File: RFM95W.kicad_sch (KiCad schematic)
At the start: 2 parts

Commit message: ongoing add MCU and radio.
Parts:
- added AE1: 915mhz antenna, ProjectLib:915MHz_spring_antenna, symbol Device:Antenna
- R?: value 10k -> 10k 1%
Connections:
- net ANT: no longer names the net of U?.9 (ANT)
- net ANT: now also AE1.1 (A)

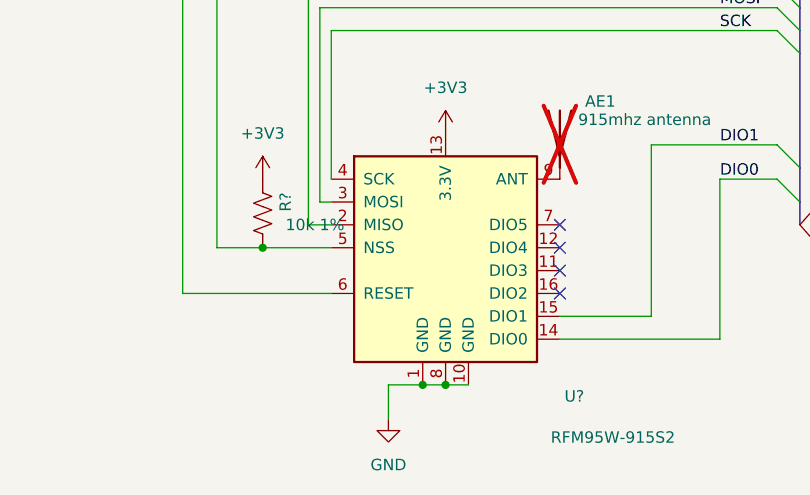
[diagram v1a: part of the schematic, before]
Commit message: ERC passing, Crytals not specified. Considering reverse polarity safeguard.
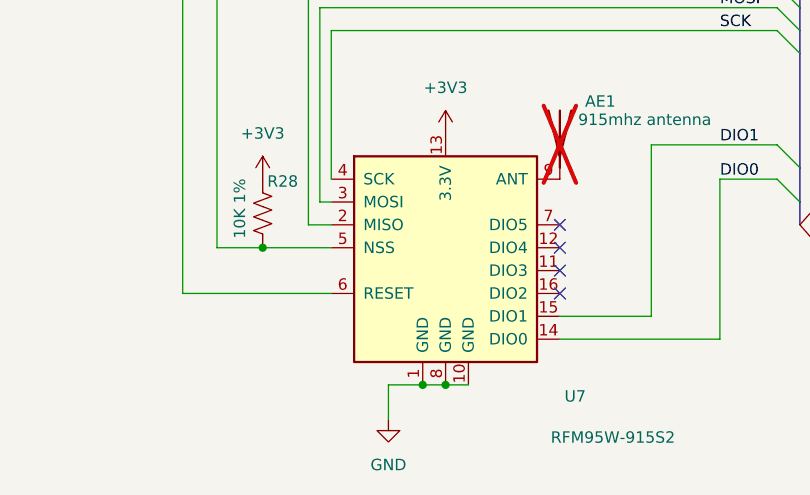
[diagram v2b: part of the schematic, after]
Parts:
- removed R?: 10k 1%, ProjectLib:R_0603_1608Metric, symbol ProjectLib:R_US
- added R28: 10K 1%, symbol Device:R_US
- gave numbers to parts that had none: 1
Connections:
- net +3V3: now also R28.1
- net NSS: now also R28.2
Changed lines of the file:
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@@
+	)
+	(junction
+		(at 115.57 100.33)
+		(diameter 0)
+		(color 0 0 0 0)
 	)
 	(junction
@@
 		(color 0 0 0 0)
 	)
-	(junction
-		(at 115.57 100.33)
-		(diameter 0)
-		(color 0 0 0 0)
-	)
 	(no_connect
 		(at 128.27 87.63)
@@
 		)
 	)
-	(wire
-		(pts
-			(xy 95.25 85.09) (xy 90.17 85.09)
-		)
-		(stroke
-			(width 0)
-			(type default)
-		)
-	)
 	(bus
 		(pts
@@
 	(wire
 		(pts
-			(xy 102.87 85.09) (xy 95.25 85.09)
-		)
-		(stroke
-			(width 0)
-			(type default)
-		)
-	)
-	(wire
-		(pts
 			(xy 102.87 82.55) (xy 100.33 82.55)
 		)
@@
 		(pts
 			(xy 154.94 80.01) (xy 154.94 82.55)
+		)
+		(stroke
+			(width 0)
+			(type default)
+		)
+	)
+	(wire
+		(pts
+			(xy 95.25 85.09) (xy 102.87 85.09)
+		)
+		(stroke
+			(width 0)
+			(type default)
+		)
+	)
+	(wire
+		(pts
+			(xy 90.17 85.09) (xy 95.25 85.09)
 		)
 		(stroke
@@
 	)
 	(symbol
+		(lib_id "Device:R_US")
+		(at 95.25 81.28 0)
+		(unit 1)
+		(exclude_from_sim no)
+		(in_bom yes)
+		(on_board yes)
+		(dnp no)
+		(property "Reference" "R28"
+			(at 95.758 77.724 0)
+			(effects
+				(font
+					(size 1.27 1.27)
+				)
+				(justify left)
+			)
+		)
+		(property "Value" "10K 1%"
+			(at 92.71 84.074 90)
+			(effects
+				(font
+					(size 1.27 1.27)
+				)
+				(justify left)
+			)
+		)
+		(property "Footprint" ""
+			(at 96.266 81.534 90)
+			(effects
+				(font
+					(size 1.27 1.27)
+				)
+				(hide yes)
+			)
+		)
+		(property "Datasheet" "~"
+			(at 95.25 81.28 0)
+			(effects
+				(font
+					(size 1.27 1.27)
+				)
+				(hide yes)
+			)
+		)
+		(property "Description" "Resistor, US symbol"
+			(at 95.25 81.28 0)
+			(effects
+				(font
+					(size 1.27 1.27)
+				)
+				(hide yes)
+			)
+		)
+		(pin "2"
+		)
+		(pin "1"
+		)
+		(instances
+			(project ""
+				(path "/0c2d0c14-8850-4a30-bb78-b2f40cb442ba/2db29b35-1005-45eb-b852-0b853354466f"
+					(reference "R28")
+					(unit 1)
+				)
+			)
+		)
+	)
+	(symbol
 		(lib_id "power:+3V3")
 		(at 95.25 77.47 0)
@@
 		(dnp no)
 		(fields_autoplaced yes)
-		(property "Reference" "#PWR?"
+		(property "Reference" "#PWR0102"
 			(at 95.25 81.28 0)
 			(effects
@@
 			(project "SensorProject_t16-pcb"
 				(path "/0c2d0c14-8850-4a30-bb78-b2f40cb442ba/2db29b35-1005-45eb-b852-0b853354466f"
-					(reference "#PWR?")
+					(reference "#PWR0102")
 					(unit 1)
 				)
@@
 		(dnp no)
 		(fields_autoplaced yes)
-		(property "Reference" "#PWR?"
+		(property "Reference" "#PWR0103"
 			(at 109.22 110.49 0)
 			(effects
@@
 			(project "SensorProject_t16-pcb"
 				(path "/0c2d0c14-8850-4a30-bb78-b2f40cb442ba/2db29b35-1005-45eb-b852-0b853354466f"
-					(reference "#PWR?")
+					(reference "#PWR0103")
 					(unit 1)
 				)
@@
 		(dnp no)
 		(fields_autoplaced yes)
-		(property "Reference" "#PWR?"
+		(property "Reference" "#PWR0101"
 			(at 115.57 76.2 0)
 			(effects
@@
 			(project "SensorProject_t16-pcb"
 				(path "/0c2d0c14-8850-4a30-bb78-b2f40cb442ba/2db29b35-1005-45eb-b852-0b853354466f"
-					(reference "#PWR?")
+					(reference "#PWR0101")
 					(unit 1)
 				)
@@
 		(on_board yes)
 		(dnp no)
-		(property "Reference" "U?"
+		(property "Reference" "U7"
 			(at 128.778 101.6 0)
 			(effects
@@
 			(project "SensorProject_t16-pcb"
 				(path "/0c2d0c14-8850-4a30-bb78-b2f40cb442ba/2db29b35-1005-45eb-b852-0b853354466f"
-					(reference "U?")
+					(reference "U7")
 					(unit 1)
 				)
-			)
-		)
-	)
-	(symbol
-		(lib_id "ProjectLib:R_US")
-		(at 95.25 81.28 0)
-		(unit 1)
-		(exclude_from_sim no)
-		(in_bom yes)
-		(on_board yes)
-		(dnp no)
-		(fields_autoplaced yes)
-		(property "Reference" "R?"
-			(at 97.79 80.01 90)
-			(effects
-				(font
-					(size 1.27 1.27)
-				)
-			)
-		)
-		(property "Value" "10k 1%"
-			(at 97.79 82.55 0)
-			(effects
-				(font
-					(size 1.27 1.27)
-				)
-				(justify left)
-			)
-		)
-		(property "Footprint" "ProjectLib:R_0603_1608Metric"
-			(at 96.266 81.534 90)
-			(effects
-				(font
-					(size 1.27 1.27)
-				)
-				(hide yes)
-			)
-		)
-		(property "Datasheet" "~"
-			(at 95.25 81.28 0)
-			(effects
-				(font
-					(size 1.27 1.27)
-				)
-				(hide yes)
-			)
-		)
-		(property "Description" "Resistor, US symbol"
-			(at 95.25 81.28 0)
-			(effects
-				(font
-					(size 1.27 1.27)
-				)
-				(hide yes)
-			)
-		)
-		(property "MountType" "SMT"
-			(at 95.25 81.28 0)
-			(effects
-				(font
-					(size 1.27 1.27)
-				)
-				(hide yes)
-			)
-		)
-		(property "Manufacturer" ""
-			(at 95.25 81.28 0)
-			(effects
-				(font
-					(size 1.27 1.27)
-				)
-				(hide yes)
-			)
-		)
-		(property "MfgPart" ""
-			(at 95.25 81.28 0)
-			(effects
-				(font
-					(size 1.27 1.27)
-				)
-				(hide yes)
-			)
-		)
-		(property "Notes" ""
-			(at 95.25 81.28 0)
-			(effects
-				(font
-					(size 1.27 1.27)
-				)
-				(hide yes)
-			)
-		)
-		(pin "1"
-		)
-		(pin "2"
-		)
-		(instances
-			(project "SensorProject_t16-pcb"
-				(path "/0c2d0c14-8850-4a30-bb78-b2f40cb442ba/2db29b35-1005-45eb-b852-0b853354466f"
-					(reference "R?")
-					(unit 1)
-				)

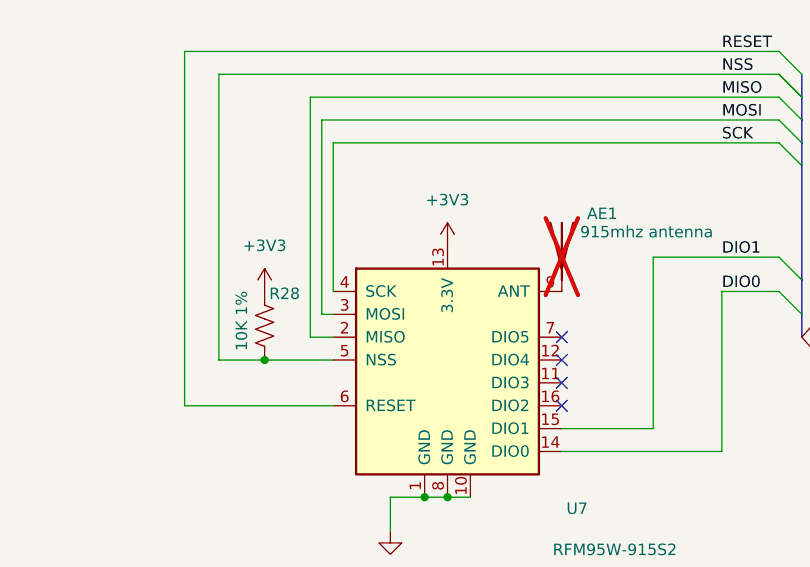
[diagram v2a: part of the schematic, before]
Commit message: f401.kicad_sch mostly complete other than xtals. Considering switch to f411 for memory, FPU, and generation 2 oscillator that gives better crystal choices.
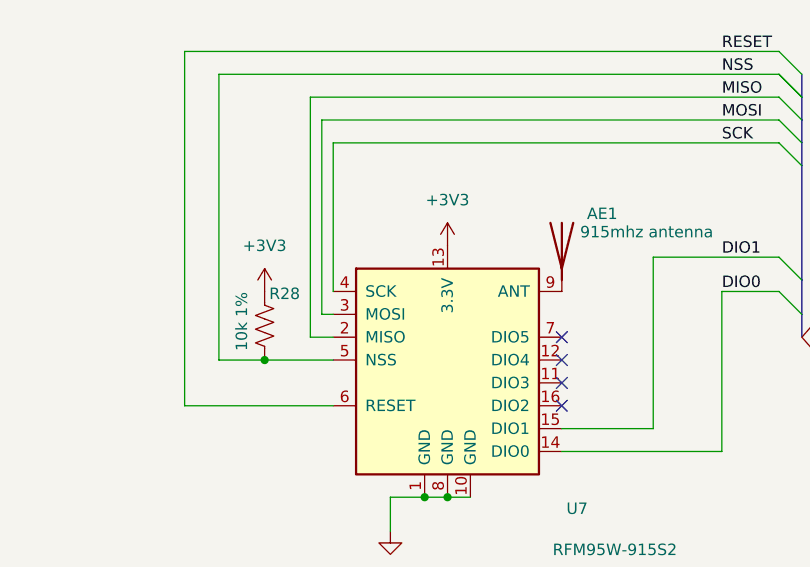
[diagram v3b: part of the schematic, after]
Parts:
- AE1: footprint ProjectLib:915MHz_spring_antenna -> (none); Manufacturer NiceRF -> UTC; MfgPart sw915-th06 -> AA066; MountType PTH -> SMT; now fitted
- R28: value 10K 1% -> 10k 1%; footprint (none) -> ProjectLib:R_0201_0603Metric; MountType (none) -> SMT
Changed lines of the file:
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@@
 		(in_bom yes)
 		(on_board yes)
-		(dnp yes)
+		(dnp no)
 		(property "Reference" "AE1"
 			(at 131.064 68.834 0)
@@
 			)
 		)
-		(property "Footprint" "ProjectLib:915MHz_spring_antenna"
+		(property "Footprint" ""
 			(at 128.27 72.39 0)
 			(effects
@@
 			)
 		)
-		(property "Datasheet" "https://www.nicerf.com/rf-antenna/915mhz-spring-antenna-sw915-th06.html"
+		(property "Datasheet" "https://www.unictron.com/wireless-communications/wp-content/uploads/2021/04/AA066.pdf"
 			(at 128.27 72.39 0)
 			(effects
@@
 			)
 		)
-		(property "Description" "Antenna"
+		(property "Description" "Chip Antenna"
 			(at 128.27 72.39 0)
 			(effects
@@
 			)
 		)
-		(property "Manufacturer" "NiceRF"
+		(property "Manufacturer" "UTC"
 			(at 128.27 72.39 0)
 			(effects
@@
 			)
 		)
-		(property "MfgPart" "sw915-th06"
+		(property "MfgPart" "AA066"
 			(at 128.27 72.39 0)
 			(effects
@@
 			)
 		)
-		(property "MountType" "PTH"
+		(property "MountType" "SMT"
 			(at 128.27 72.39 0)
 			(effects
@@
 			)
 		)
-		(property "Value" "10K 1%"
+		(property "Value" "10k 1%"
 			(at 92.71 84.074 90)
 			(effects
@@
 			)
 		)
-		(property "Footprint" ""
+		(property "Footprint" "ProjectLib:R_0201_0603Metric"
 			(at 96.266 81.534 90)
 			(effects
@@
 			(at 95.25 81.28 0)
 			(effects
+				(font
+					(size 1.27 1.27)
+				)
+				(hide yes)
+			)
+		)
+		(property "MountType" "SMT"
+			(at 95.25 81.28 0)
+			(effects

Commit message: layout with F411 roughly good but needs work.
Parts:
- AE1: footprint (none) -> ProjectLib:915MHz_spring_antenna
- R28: footprint ProjectLib:R_0201_0603Metric -> ProjectLib:R_0603_1608Metric
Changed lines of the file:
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@@
 			)
 		)
-		(property "Footprint" ""
+		(property "Footprint" "ProjectLib:915MHz_spring_antenna"
 			(at 128.27 72.39 0)
 			(effects
@@
 			)
 		)
-		(property "Footprint" "ProjectLib:R_0201_0603Metric"
+		(property "Footprint" "ProjectLib:R_0603_1608Metric"
 			(at 96.266 81.534 90)
 			(effects

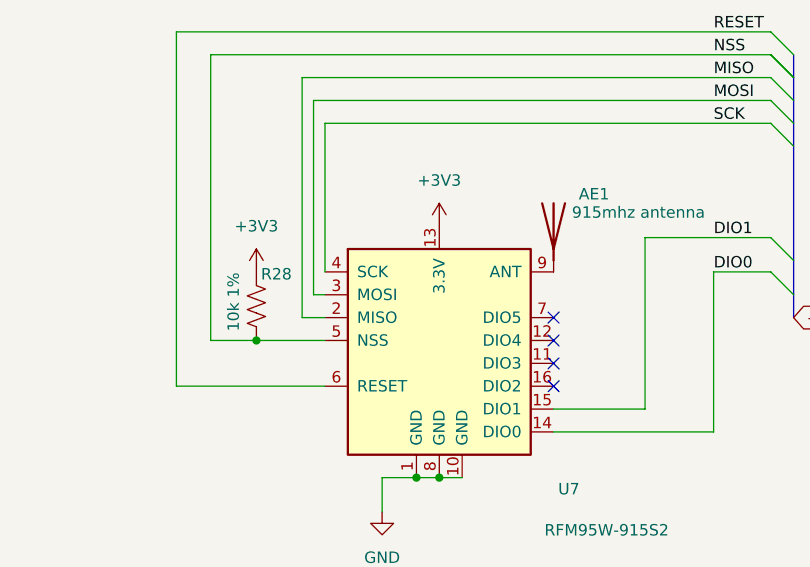
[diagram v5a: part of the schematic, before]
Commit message: near complete, DRC good, ERC has a spurious error about ground on Y1.
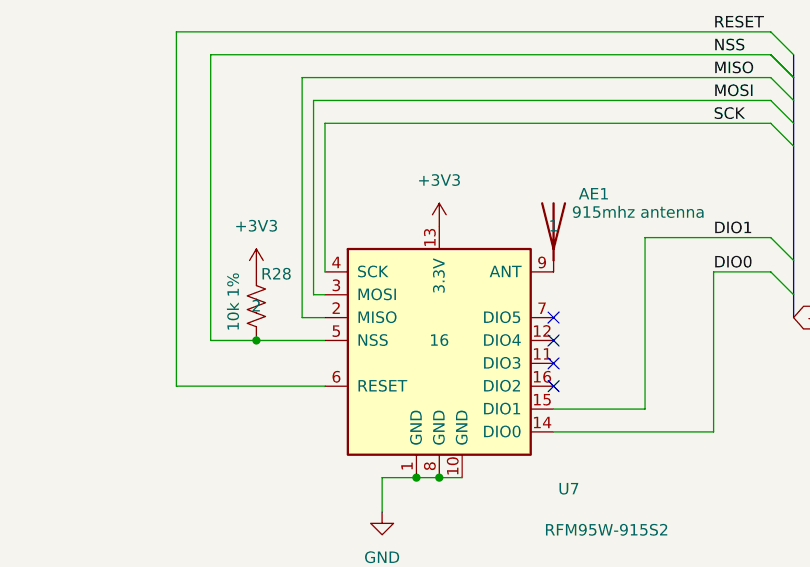
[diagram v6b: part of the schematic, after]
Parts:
- AE1: Manufacturer UTC -> G-NiceRF; MfgPart AA066 -> SW915-TH06; MountType SMT -> PTH; pads (none) -> 1
- R28: pads (none) -> 2
- U7: pads (none) -> 16
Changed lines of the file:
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@@
 			)
 		)
-		(property "Datasheet" "~"
-			(at 128.27 72.39 0)
-			(effects
-				(font
-					(size 1.27 1.27)
-				)
-				(hide yes)
-			)
-		)
-		(property "Description" "Antenna"
-			(at 128.27 72.39 0)
-			(effects
-				(font
-					(size 1.27 1.27)
-				)
-				(hide yes)
-			)
-		)
-		(property "Manufacturer" "UTC"
-			(at 128.27 72.39 0)
-			(effects
-				(font
-					(size 1.27 1.27)
-				)
-				(hide yes)
-			)
-		)
-		(property "MfgPart" "AA066"
-			(at 128.27 72.39 0)
-			(effects
-				(font
-					(size 1.27 1.27)
-				)
-				(hide yes)
-			)
-		)
-		(property "MountType" "SMT"
+		(property "Datasheet" "https://www.nicerf.com/rf-antenna/915mhz-spring-antenna-sw915-th06.html"
+			(at 128.27 72.39 0)
+			(effects
+				(font
+					(size 1.27 1.27)
+				)
+				(hide yes)
+			)
+		)
+		(property "Description" "spring antenna"
+			(at 128.27 72.39 0)
+			(effects
+				(font
+					(size 1.27 1.27)
+				)
+				(hide yes)
+			)
+		)
+		(property "Manufacturer" "G-NiceRF"
+			(at 128.27 72.39 0)
+			(effects
+				(font
+					(size 1.27 1.27)
+				)
+				(hide yes)
+			)
+		)
+		(property "MfgPart" "SW915-TH06"
+			(at 128.27 72.39 0)
+			(effects
+				(font
+					(size 1.27 1.27)
+				)
+				(hide yes)
+			)
+		)
+		(property "MountType" "PTH"
 			(at 128.27 72.39 0)
 			(effects
@@
 				)
 				(hide yes)
+			)
+		)
+		(property "pads" "1"
+			(at 128.27 72.39 0)
+			(effects
+				(font
+					(size 1.27 1.27)
+				)
 			)
 		)
@@
 				)
 				(hide yes)
+			)
+		)
+		(property "pads" "2"
+			(at 95.25 81.28 0)
+			(effects
+				(font
+					(size 1.27 1.27)
+				)
 			)
 		)
@@
 			)
 		)
+		(property "pads" "16"
+			(at 115.57 85.09 0)
+			(effects
+				(font
+					(size 1.27 1.27)
+				)
+			)
+		)

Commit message: cleanup, ready to submit.
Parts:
- AE1: now not fitted
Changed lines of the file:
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@@
 		(in_bom yes)
 		(on_board yes)
-		(dnp no)
+		(dnp yes)
 		(property "Reference" "AE1"
 			(at 131.064 68.834 0)
@@
 					(size 1.27 1.27)
 				)
+				(hide yes)
 			)
 		)
@@
 					(size 1.27 1.27)
 				)
+				(hide yes)
 			)
 		)
@@
 			)
 		)
-		(property "Description" "Low power long range transceiver module, SPI and parallel interface, 915 MHz, spreading factor 6 to12, bandwidth 7.8 to 500kHz, -111 to -148 dBm, SMD-16, DIP-16"
+		(property "Description" "LoRa module, SPI, 915 MHz"
 			(at 115.57 85.09 0)
 			(effects

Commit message: As made,  t16-F411 v0.2.0 2025-05, with added notes about needed fixes and results from some testing.
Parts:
- R28: Manufacturer (none) -> Vishay; MfgPart (none) -> CRCW060310K0FKEA
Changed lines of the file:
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@@
 			)
 		)
-		(property "Datasheet" "~"
+		(property "Datasheet" ""
 			(at 95.25 81.28 0)
 			(effects
@@
 			(at 95.25 81.28 0)
 			(effects
+				(font
+					(size 1.27 1.27)
+				)
+				(hide yes)
+			)
+		)
+		(property "Manufacturer" "Vishay"
+			(at 95.25 81.28 0)
+			(effects
+				(font
+					(size 1.27 1.27)
+				)
+				(hide yes)
+			)
+		)
+		(property "MfgPart" "CRCW060310K0FKEA"
+			(at 95.25 81.28 0)
+			(effects
